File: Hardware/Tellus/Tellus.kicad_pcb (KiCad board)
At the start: 4 copper layers, 77.1 x 76.2 mm, 38 parts, among them J1 Conn_01x02_Female, J10 Conn_01x02_Female, J11 Conn_01x04_Female, J12 Conn_01x04_Female, J13 Conn_01x03_Female, J14 Conn_01x03_Female, J2 Conn_01x02_Female, J3 Conn_01x02_Female, J4 Conn_01x02_Female, J5 Conn_01x02_Female, J6 Conn_01x02_Female, J7 Conn_01x02_Female, J8 Conn_01x02_Female, J9 Conn_01x02_Female, U1 A3909, U2 AMS1117-3.3, U3 A3909, U4 A3909, U5 DEV-16771, U6 MC6470, U7 ICM-42670-P

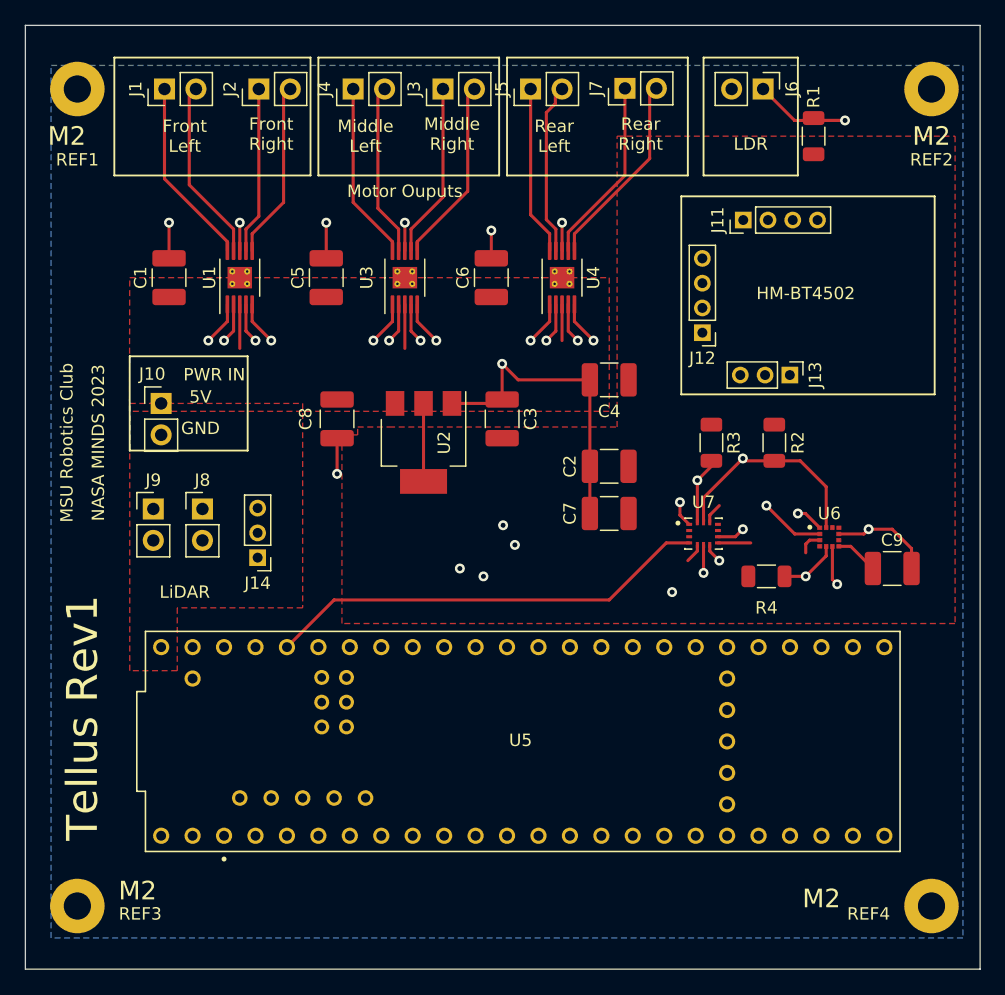
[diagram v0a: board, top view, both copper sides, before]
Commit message: PCB Updates
Re-Layered PCB to match Signal, PWR, GND, Signal suggestion. Cleaned up power connections, Bluetooth saddle, and LiDAR mounts.

Fixed the following DRC Violations/Warnings:
No Footprint assigned for Mounting holes
- Fixed by adding them in the schematic.

Unconnected 3.3V Terminals on Teensy
- Fixed Symbol in schematic that had them on top of each other. The teensy spec does not recommend tying these together.

No net assigned for Motor Driver EP
-Modified Symbol in schematic to include the EP, and connected it to GND, as suggested in the data sheet.
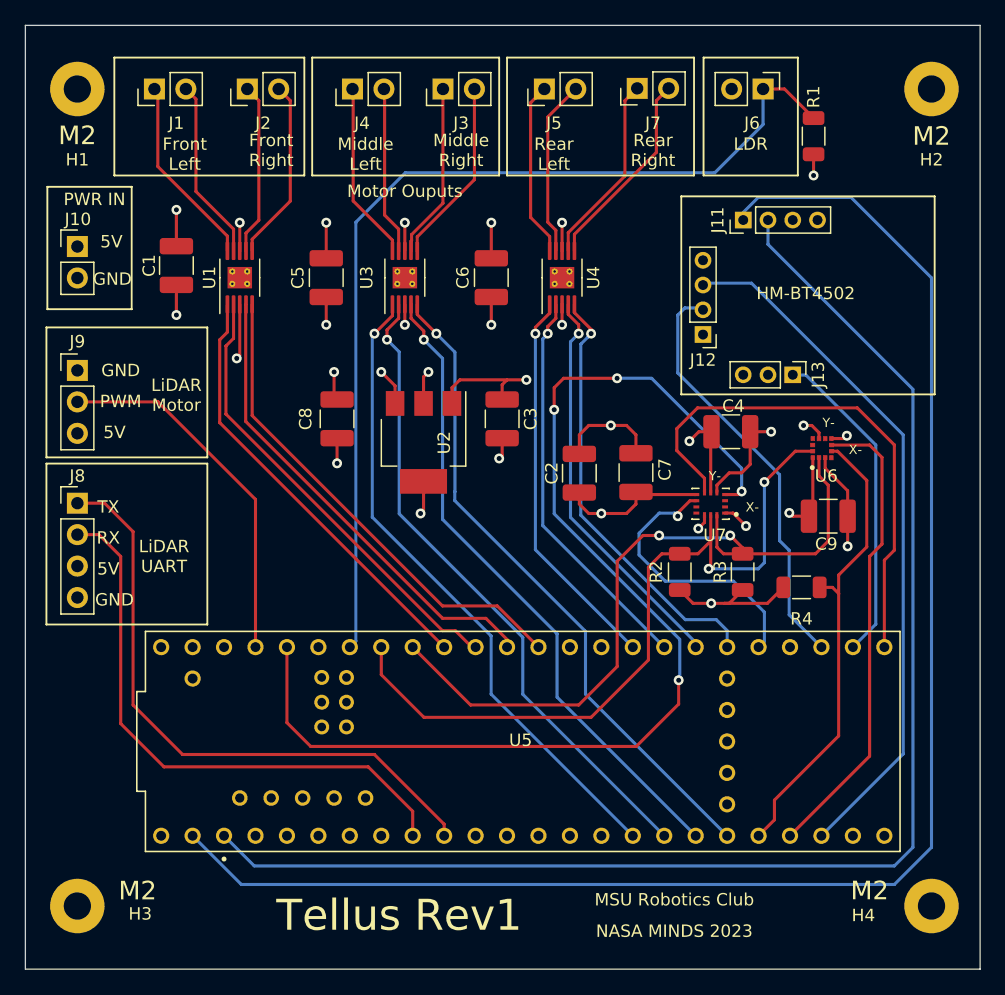
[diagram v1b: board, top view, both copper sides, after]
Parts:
- removed J14: Conn_01x03_Female, Connector_PinHeader_2.00mm:PinHeader_1x03_P2.00mm_Vertical
- J8: value Conn_01x02_Female -> Conn_01x04_Female; footprint Connector_PinHeader_2.54mm:PinHeader_1x02_P2.54mm_Vertical -> Connector_PinHeader_2.54mm:PinHeader_1x04_P2.54mm_Vertical
- J9: value Conn_01x02_Female -> Conn_01x03_Female; footprint Connector_PinHeader_2.54mm:PinHeader_1x02_P2.54mm_Vertical -> Connector_PinHeader_2.54mm:PinHeader_1x03_P2.54mm_Vertical
- moved J10 14.4 mm to (121.5, 91.5)
- moved R2 12.9 mm to (170.2, 117.8), turned to 90 degrees
- moved J9 12.8 mm to (121.5, 101.5)
- moved R3 10.7 mm to (175.2, 117.8), turned to 90 degrees
- moved C4 10.7 mm to (174.3, 106.4)
- moved J8 10.1 mm to (121.5, 112.2)
- moved U6 7.21 mm to (181.7, 107.8), turned to 90 degrees
- moved C9 6.67 mm to (182.2, 113.2), turned to 180 degrees
- moved C7 3.95 mm to (166.6, 109.7), turned to 90 degrees
- moved R4 2.97 mm to (180.0, 119.0)
- moved C2 2.48 mm to (162.1, 109.8), turned to 90 degrees
- moved U7 2.48 mm to (172.7, 112.2), turned to 180 degrees
- moved C1 1.15 mm to (129.5, 93.0)
- moved J5 1.11 mm to (159.2, 78.7)
- moved J7 0.99 mm to (166.7, 78.7)
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- renumbered REF1 to H1, REF2 to H2, REF3 to H3, REF4 to H4
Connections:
- J8 pad 1: 5V -> Lidar_TX
- J8 pad 2: GND -> Lidar_RX
- J9 pad 1: 5V -> GND
- J9 pad 2: GND -> Lidar_PWM
- U1 pad 11: (no net) -> GND
- U3 pad 11: (no net) -> GND
- U4 pad 11: (no net) -> GND
- U5 pad 3.3V_2: unconnected-(U5-Pad3.3V_1) -> unconnected-(U5-Pad3.3V_2)
- U5 pad 3.3V_3: unconnected-(U5-Pad3.3V_1) -> unconnected-(U5-Pad3.3V_3)
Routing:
- net INT1_ICM: track 36.0 -> 91.5 mm, vias 0 -> 4
- net LDR Out: track 129.7 -> 78.6 mm, vias 1 -> 0
- net 3.3V: track 17.7 -> 49.7 mm, vias 0 -> 10
- net FSYNC_ICM: track 17.8 -> 42.3 mm, vias 1 -> 0
- net Lidar_TX: track 33.3 -> 49.5 mm
- net Lidar_PWM: track 13.5 -> 29.6 mm
- net SDA: track 45.7 -> 59.6 mm, vias 4 -> 2
- net INTM: track 25.3 -> 38.1 mm, vias 1 -> 0
- net Lidar_RX: track 35.2 -> 46.2 mm
- net INT2_ICM: track 12.3 -> 23.0 mm
- net INTA: track 27.3 -> 37.9 mm, vias 1 -> 0
- net 5V: track 10.0 -> 20.0 mm, vias 0 -> 8
- net SCLK: track 52.9 -> 61.1 mm, vias 3 -> 2
- net TXD: track 120.8 -> 112.8 mm
- net GND: track 58.1 -> 53.2 mm, vias 12 -> 13
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- added copper zone on In1.Cu, net 3.3V
- added copper zone on In1.Cu, net 5V
- added copper zone on In2.Cu, net GND
- removed copper zone on F.Cu, net 3.3V
- removed copper zone on F.Cu, net 5V
- removed copper zone on B.Cu, net GND
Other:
- board text added: "LiDAR Motor"
- board text added: "LiDAR UART"
- board text added: "PWM"
- board text added: "RX"
- board text added: "TX"
- board text added: "X-"
- board text added: "Y-"
- board text removed: "LiDAR"

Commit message: Added Logos
Added MSU Logo and Robotics Club Logo to the front and back silkscreen layers
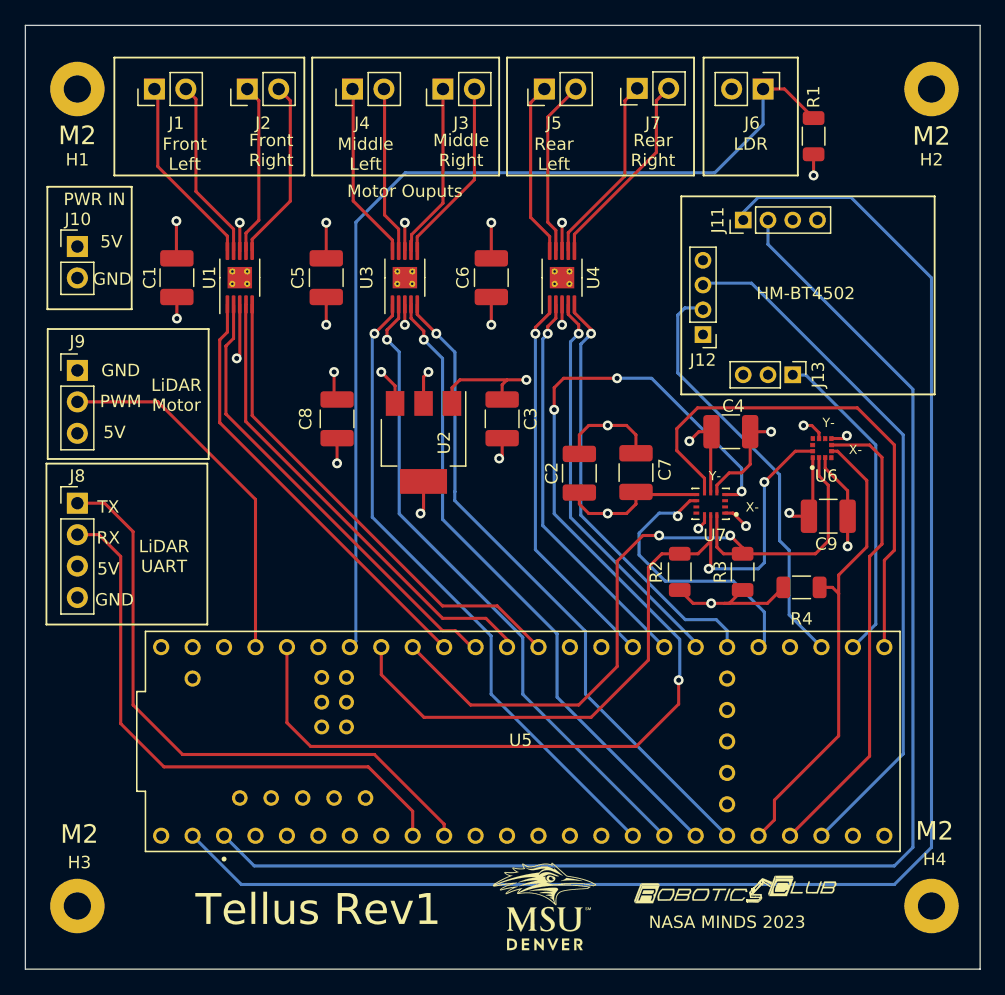
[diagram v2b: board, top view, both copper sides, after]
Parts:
- moved C1 0.98 mm to (129.5, 94.0)
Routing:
- net GND: track 53.2 -> 52.3 mm
- net 5V: track 20.0 -> 19.3 mm
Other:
- board text removed: "MSU Robotics Club"

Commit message: Cleanup
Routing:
- net GND: track 52.3 -> 50.0 mm
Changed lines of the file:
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@@
   (segment (start 180.9125 112.9375) (end 180.6 113.25) (width 0.25) (layer "F.Cu") (net 2))
   (segment (start 154.94 92.4175) (end 154.94 89.535) (width 0.25) (layer "F.Cu") (net 2))
+  (segment (start 155.194 102.235) (end 155.067 102.108) (width 0.25) (layer "F.Cu") (net 2))
+  (segment (start 152.4 102.108) (end 153.67 102.108) (width 0.25) (layer "F.Cu") (net 2))
   (segment (start 172.727614 106.426) (end 172.6625 106.491114) (width 0.25) (layer "F.Cu") (net 2))
   (segment (start 172.6625 106.491114) (end 172.6625 111.3375) (width 0.25) (layer "F.Cu") (net 2))
@@
   (segment (start 166.624 106.68) (end 166.624 108.1655) (width 0.25) (layer "F.Cu") (net 2))
   (segment (start 164.338 105.918) (end 165.862 105.918) (width 0.25) (layer "F.Cu") (net 2))
-  (segment (start 151.765 104.14) (end 151.765 102.87) (width 0.25) (layer "F.Cu") (net 2))
-  (segment (start 151.765 102.87) (end 152.4 102.235) (width 0.25) (layer "F.Cu") (net 2))
   (segment (start 129.5 91.8225) (end 129.5 89.408) (width 0.25) (layer "F.Cu") (net 2))
   (segment (start 141.605 92.4175) (end 141.605 89.535) (width 0.25) (layer "F.Cu") (net 2))
+  (segment (start 151.765 104.14) (end 151.765 102.743) (width 0.25) (layer "F.Cu") (net 2))
   (segment (start 170.942 107.188) (end 171.704 106.426) (width 0.25) (layer "F.Cu") (net 2))
-  (segment (start 152.4 102.235) (end 156.21 102.235) (width 0.25) (layer "F.Cu") (net 2))
+  (segment (start 155.067 102.108) (end 153.67 102.108) (width 0.25) (layer "F.Cu") (net 2))
+  (segment (start 155.815 103.8225) (end 155.815 102.856) (width 0.25) (layer "F.Cu") (net 2))
   (segment (start 164.338 105.918) (end 162.814 105.918) (width 0.25) (layer "F.Cu") (net 2))
   (segment (start 180.1625 105.922321) (end 180.834821 105.922321) (width 0.25) (layer "F.Cu") (net 2))
@@
   (segment (start 162.052 106.68) (end 162.052 108.216713) (width 0.25) (layer "F.Cu") (net 2))
   (segment (start 180.834821 105.922321) (end 181.4125 106.5) (width 0.25) (layer "F.Cu") (net 2))
+  (segment (start 155.815 102.856) (end 155.194 102.235) (width 0.25) (layer "F.Cu") (net 2))
   (segment (start 181.4125 106.5) (end 181.4125 106.985) (width 0.25) (layer "F.Cu") (net 2))
   (segment (start 174.468 113) (end 173.825 113) (width 0.25) (layer "F.Cu") (net 2))
+  (segment (start 151.765 102.743) (end 152.4 102.108) (width 0.25) (layer "F.Cu") (net 2))
   (segment (start 179.012299 112.987701) (end 179.274598 113.25) (width 0.25) (layer "F.Cu") (net 2))
-  (segment (start 155.815 103.8225) (end 155.815 102.63) (width 0.25) (layer "F.Cu") (net 2))
   (segment (start 175.514 114.046) (end 174.468 113) (width 0.25) (layer "F.Cu") (net 2))
-  (segment (start 156.21 102.235) (end 157.7755 102.235) (width 0.25) (layer "F.Cu") (net 2))
   (segment (start 171.704 106.426) (end 172.727614 106.426) (width 0.25) (layer "F.Cu") (net 2))
   (segment (start 147.955 91.8175) (end 147.955 89.535) (width 0.25) (layer "F.Cu") (net 2))
@@
   (segment (start 179.274598 113.25) (end 180.6 113.25) (width 0.25) (layer "F.Cu") (net 2))
   (segment (start 142.48 106.9475) (end 142.48 108.98) (width 0.25) (layer "F.Cu") (net 2))
-  (segment (start 155.815 102.63) (end 156.21 102.235) (width 0.25) (layer "F.Cu") (net 2))
   (segment (start 134.62 91.8175) (end 134.62 89.535) (width 0.25) (layer "F.Cu") (net 2))
   (segment (start 162.814 105.918) (end 162.052 106.68) (width 0.25) (layer "F.Cu") (net 2))
@@
   (via (at 179.012299 112.987701) (size 0.8) (drill 0.4) (layers "F.Cu" "B.Cu") (net 2))
   (via (at 141.605 89.535) (size 0.8) (drill 0.4) (layers "F.Cu" "B.Cu") (net 2))
-  (via (at 157.7755 102.235) (size 0.8) (drill 0.4) (layers "F.Cu" "B.Cu") (free) (net 2))
+  (via (at 153.67 102.108) (size 0.8) (drill 0.4) (layers "F.Cu" "B.Cu") (free) (net 2))
   (via (at 170.942 107.188) (size 0.8) (drill 0.4) (layers "F.Cu" "B.Cu") (net 2))
   (via (at 175.514 114.046) (size 0.8) (drill 0.4) (layers "F.Cu" "B.Cu") (net 2))

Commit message: Final Edits and Manufacturer File Generation
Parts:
- U1, U3, U4: footprint Package_SO:MSOP-10-1EP_3x3mm_P0.5mm_EP1.73x1.98mm_ThermalVias -> Package_SO:SSOP-10_3.9x4.9mm_P1.00mm
- U2: footprint Package_TO_SOT_SMD:SOT-223-3_TabPin2 -> Package_TO_SOT_SMD:SOT-89-3
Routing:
- net 3.3V: track 49.7 -> 56.0 mm
- net 5V: track 19.3 -> 21.1 mm
- net GND: track 50.0 -> 51.8 mm
- net Lidar_PWM: track 29.6 -> 30.6 mm
- net Rear Right Control 2: track 34.9 -> 33.9 mm
- net SDA: track 59.6 -> 60.5 mm
- net Rear Right Control 1: track 32.5 -> 31.6 mm
- net Rear Left Control 1: track 31.4 -> 30.6 mm
- net Mid Right Control 2: track 53.3 -> 52.5 mm
- net Mid Left Control 1: track 52.3 -> 51.5 mm
- net Net-(J7-Pad2): track 16.3 -> 15.5 mm
- net Net-(J5-Pad1): track 14.2 -> 13.4 mm
- net Net-(J4-Pad1): track 14.4 -> 13.6 mm
- net Net-(J3-Pad2): track 15.0 -> 14.2 mm
- net Net-(J2-Pad2): track 14.7 -> 13.9 mm
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- added copper zone on In2.Cu, net 3.3V
- added copper zone on In2.Cu, net 5V
- added copper zone on In1.Cu, net GND
- removed copper zone on In1.Cu, net 3.3V
- removed copper zone on In1.Cu, net 5V
- removed copper zone on In2.Cu, net GND
